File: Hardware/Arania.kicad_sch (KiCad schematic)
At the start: 9 parts, among them J14 LASER, J25 Alimentacion, J26 Masa, J7 Salidas, Q1 MMBT3904

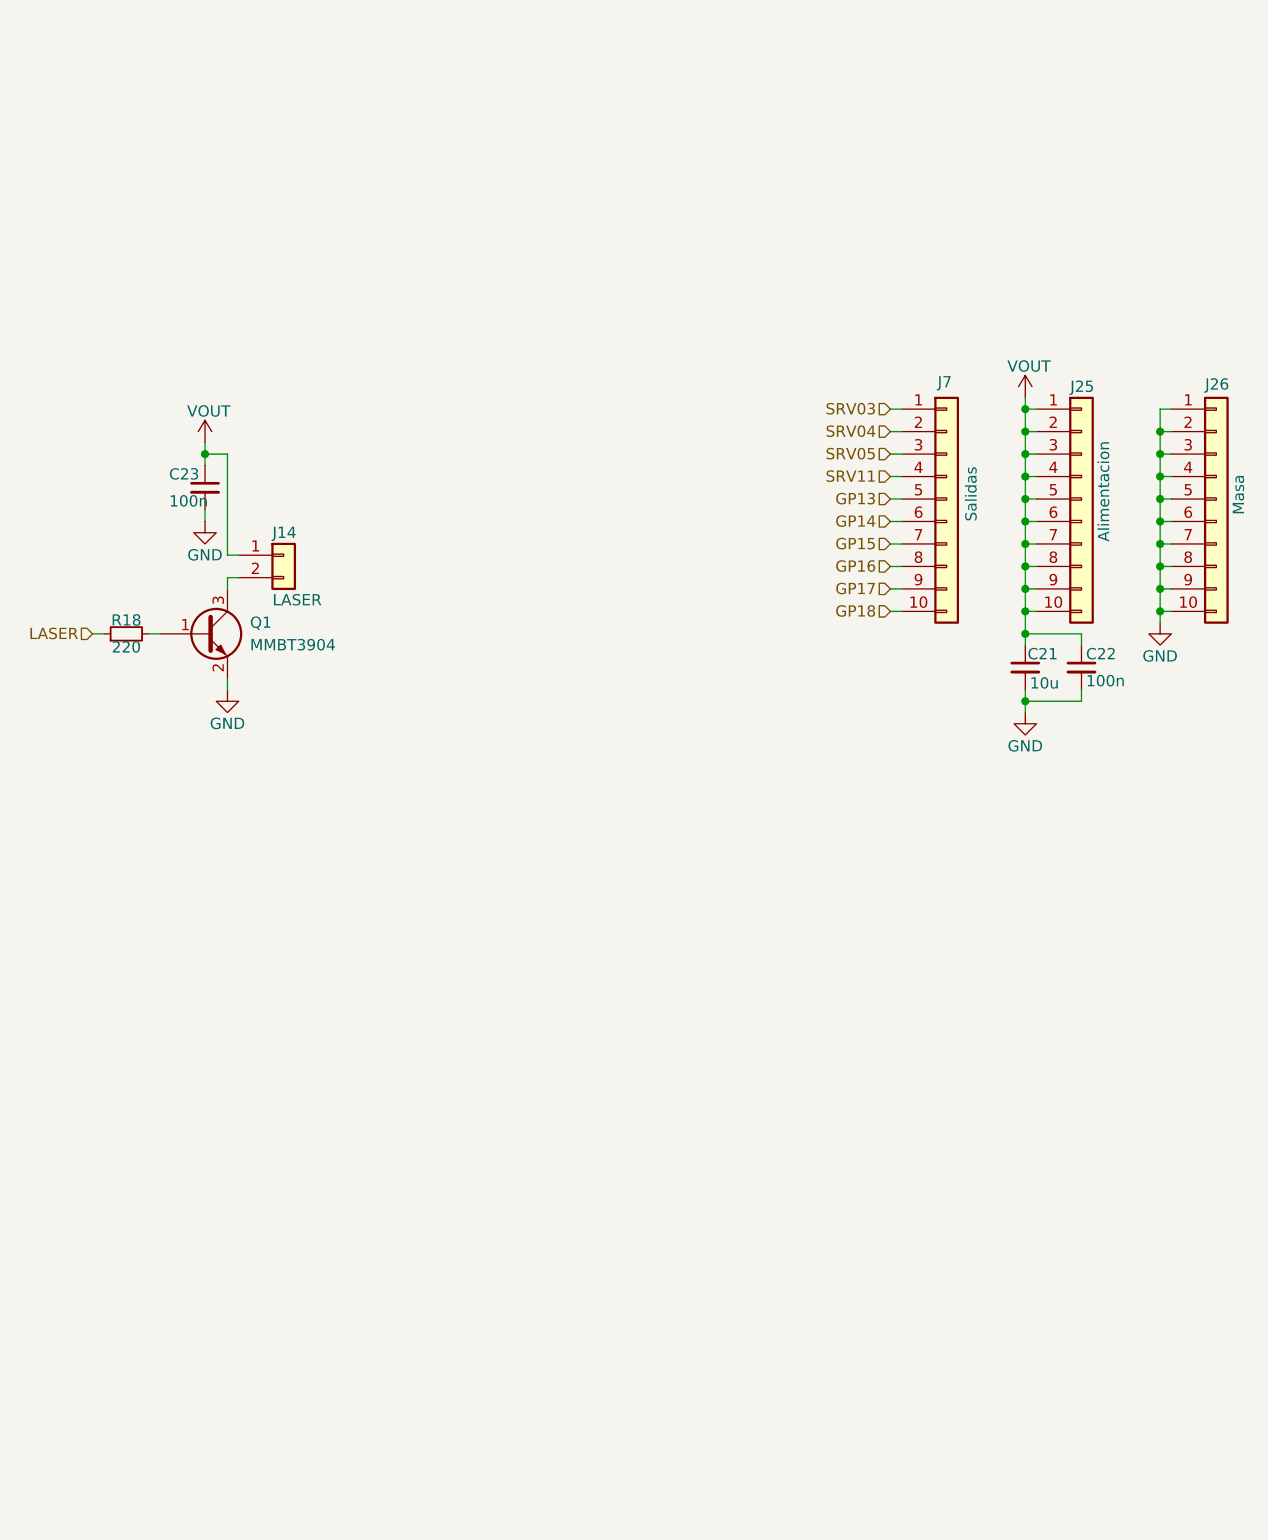
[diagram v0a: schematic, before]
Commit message: Cambio todos los conectores a SMD
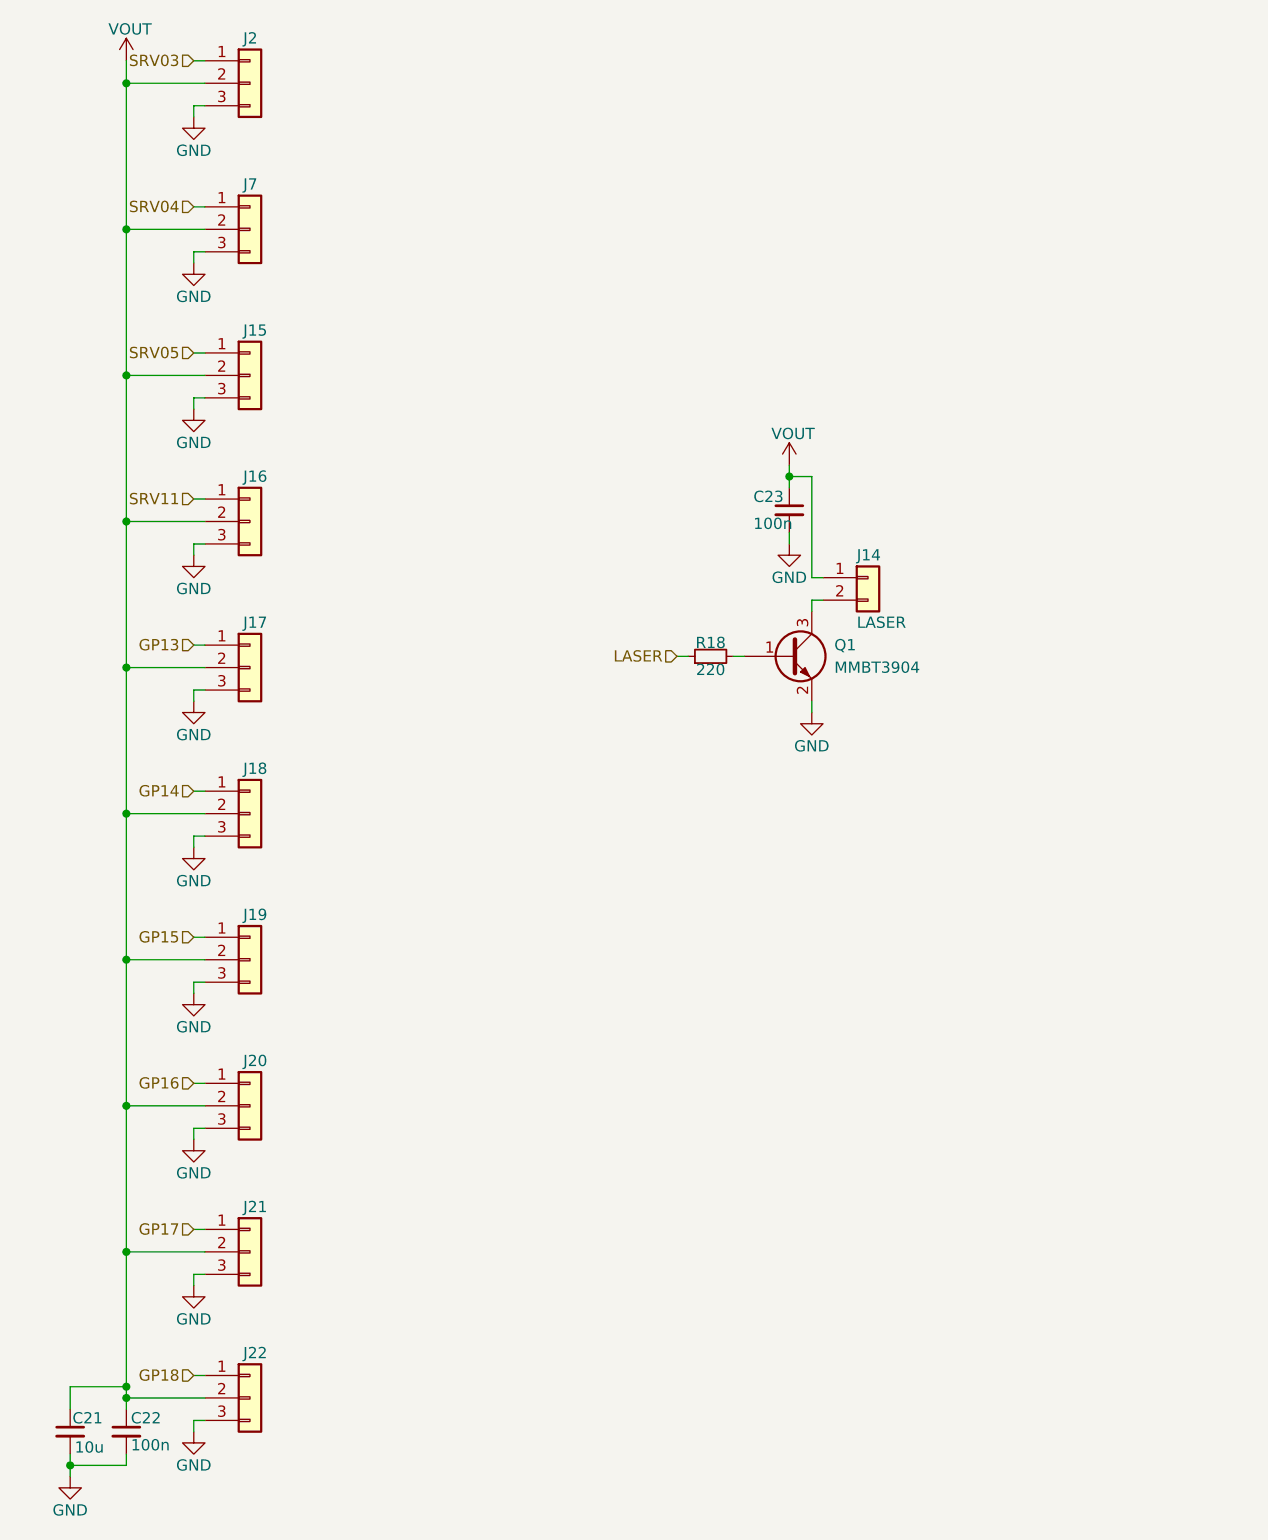
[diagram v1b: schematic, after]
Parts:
- removed J25: Alimentacion, Connector_PinHeader_2.54mm:PinHeader_1x10_P2.54mm_Vertical, symbol Connector_Generic:Conn_01x10
- removed J26: Masa, Connector_PinHeader_2.54mm:PinHeader_1x10_P2.54mm_Vertical, symbol Connector_Generic:Conn_01x10
- removed J7: Salidas, Connector_PinHeader_2.54mm:PinHeader_1x10_P2.54mm_Vertical, symbol Connector_Generic:Conn_01x10
- added J15, J16, J17, J18, J19, J2, J20, J21, J22, J7: Conn_01x03, footprints:SAMTEC_TSM-103-01-TM-SV-P-TR, symbol Connector_Generic:Conn_01x03
- J14: footprint Connector_PinHeader_2.54mm:PinHeader_1x02_P2.54mm_Vertical -> footprints:SAMTEC_SSM-102-L-SV-K-TR; PartNumber (none) -> SSM-102-L-SV-K-TR; PurchaseLink (none) -> https://www.digikey.com/en/products/detail/samtec-inc/SSM-1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
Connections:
- net GND: now also J15.3 (Pin_3), J16.3 (Pin_3), J17.3 (Pin_3), J18.3 (Pin_3), J19.3 (Pin_3), J2.3 (Pin_3), J20.3 (Pin_3), J21.3 (Pin_3), J22.3 (Pin_3), J7.3 (Pin_3)
- net GP13: now also J17.1 (Pin_1)
- net GP14: now also J18.1 (Pin_1)
- net GP15: now also J19.1 (Pin_1)
- net GP16: now also J20.1 (Pin_1)
- net GP17: now also J21.1 (Pin_1)
- net GP18: now also J22.1 (Pin_1)
- net SRV03: now also J2.1 (Pin_1)
- net SRV04: now also J7.1 (Pin_1)
- net SRV05: now also J15.1 (Pin_1)
- net SRV11: now also J16.1 (Pin_1)
- net VOUT: now also J15.2 (Pin_2), J16.2 (Pin_2), J17.2 (Pin_2), J18.2 (Pin_2), J19.2 (Pin_2), J2.2 (Pin_2), J20.2 (Pin_2), J21.2 (Pin_2), J22.2 (Pin_2), J7.2 (Pin_2)
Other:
- moved on the sheet: C21, C22, C23, J14, Q1, R18

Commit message: Correcciones en el ruteo, agrego fiduciales, 3D y serigrafía
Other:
- company: (none) -> Newsan
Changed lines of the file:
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@@
 	(title_block
 		(title "Archi Bot")
-		(date "2024-07-18")
-		(rev "1.1")
+		(date "2024-09-27")
+		(rev "1.2")
+		(company "Newsan")
 	)
 	(junction

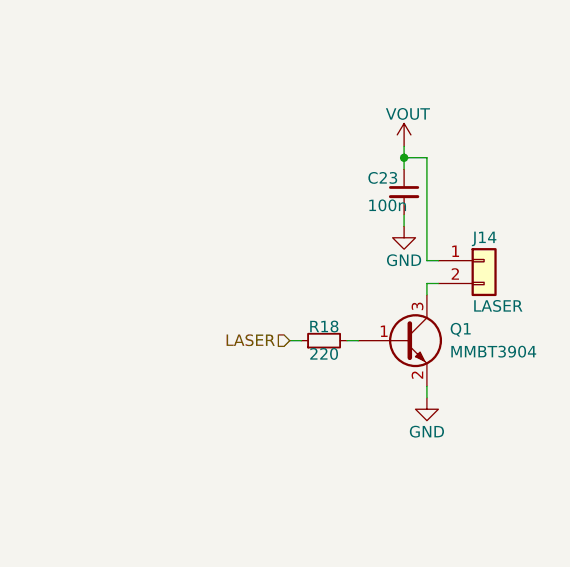
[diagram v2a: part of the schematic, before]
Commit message: Agrego test points, cambio conectores, finalizo v1.2
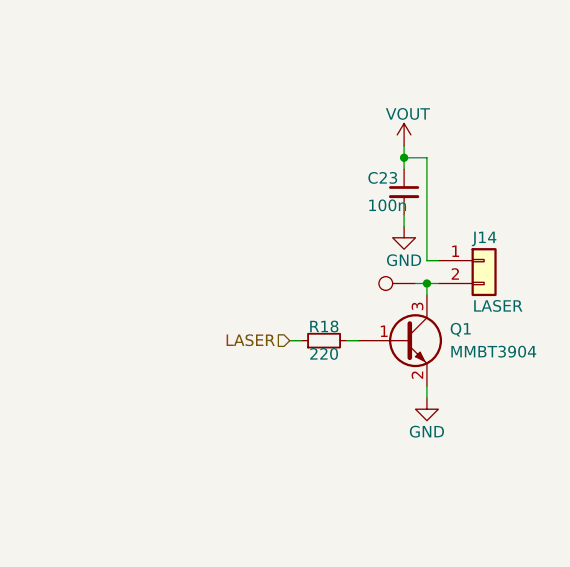
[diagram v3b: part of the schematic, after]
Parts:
- added TP28: TestPoint, TestPoint:TestPoint_Pad_D1.0mm, symbol Connector:TestPoint
- J14: footprint footprints:SAMTEC_SSM-102-L-SV-K-TR -> footprints:SAMTEC_SSM-102-L-SV-K-TR_modif
- J15, J16, J17, J18, J19, J2, J20, J21, J22, J7: footprint footprints:SAMTEC_TSM-103-01-TM-SV-P-TR -> footprints:SAMTEC_TSM-103-01-TM-SV-P-TR_modif
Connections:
- net at J14.2 (Pin_2), Q1.3 (C): now also TP28.1
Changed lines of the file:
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@@
+	)
+	(junction
+		(at 182.88 87.63)
+		(diameter 0)
+		(color 0 0 0 0)
 	)
 	(junction
@@
 		(pts
 			(xy 114.3 180.34) (xy 113.03 180.34)
+		)
+		(stroke
+			(width 0)
+			(type default)
+		)
+	)
+	(wire
+		(pts
+			(xy 181.61 87.63) (xy 182.88 87.63)
 		)
 		(stroke
@@
 			)
 		)
-		(property "Footprint" "footprints:SAMTEC_TSM-103-01-TM-SV-P-TR"
+		(property "Footprint" "footprints:SAMTEC_TSM-103-01-TM-SV-P-TR_modif"
 			(at 119.38 144.78 0)
 			(effects
@@
 				(path "/e63e39d7-6ac0-4ffd-8aa3-1841a4541b55/2971addb-a03b-4f30-bc70-6bc63fae2c84"
 					(reference "J20")
+					(unit 1)
+				)
+			)
+		)
+	)
+	(symbol
+		(lib_id "Connector:TestPoint")
+		(at 181.61 87.63 90)
+		(unit 1)
+		(exclude_from_sim no)
+		(in_bom yes)
+		(on_board yes)
+		(dnp no)
+		(fields_autoplaced yes)
+		(property "Reference" "TP28"
+			(at 177.0379 85.09 0)
+			(effects
+				(font
+					(size 1.27 1.27)
+				)
+				(justify left)
+				(hide yes)
+			)
+		)
+		(property "Value" "TestPoint"
+			(at 179.5779 85.09 0)
+			(effects
+				(font
+					(size 1.27 1.27)
+				)
+				(justify left)
+				(hide yes)
+			)
+		)
+		(property "Footprint" "TestPoint:TestPoint_Pad_D1.0mm"
+			(at 181.61 82.55 0)
+			(effects
+				(font
+					(size 1.27 1.27)
+				)
+				(hide yes)
+			)
+		)
+		(property "Datasheet" "~"
+			(at 181.61 82.55 0)
+			(effects
+				(font
+					(size 1.27 1.27)
+				)
+				(hide yes)
+			)
+		)
+		(property "Description" "test point"
+			(at 181.61 87.63 0)
+			(effects
+				(font
+					(size 1.27 1.27)
+				)
+				(hide yes)
+			)
+		)
+		(pin "1"
+		)
+		(instances
+			(project "ArchiBot"
+				(path "/e63e39d7-6ac0-4ffd-8aa3-1841a4541b55/2971addb-a03b-4f30-bc70-6bc63fae2c84"
+					(reference "TP28")
 					(unit 1)
 				)
@@
 			)
 		)
-		(property "Footprint" "footprints:SAMTEC_TSM-103-01-TM-SV-P-TR"
+		(property "Footprint" "footprints:SAMTEC_TSM-103-01-TM-SV-P-TR_modif"
 			(at 119.38 128.27 0)
 			(effects
@@
 			)
 		)
-		(property "Footprint" "footprints:SAMTEC_TSM-103-01-TM-SV-P-TR"
+		(property "Footprint" "footprints:SAMTEC_TSM-103-01-TM-SV-P-TR_modif"
 			(at 119.38 111.76 0)
 			(effects
@@
 			)
 		)
-		(property "Footprint" "footprints:SAMTEC_TSM-103-01-TM-SV-P-TR"
+		(property "Footprint" "footprints:SAMTEC_TSM-103-01-TM-SV-P-TR_modif"
 			(at 119.38 45.72 0)
 			(effects
@@
 			)
 		)
-		(property "Footprint" "footprints:SAMTEC_TSM-103-01-TM-SV-P-TR"
+		(property "Footprint" "footprints:SAMTEC_TSM-103-01-TM-SV-P-TR_modif"
 			(at 119.38 78.74 0)
 			(effects
@@
 			)
 		)
-		(property "Footprint" "footprints:SAMTEC_TSM-103-01-TM-SV-P-TR"
+		(property "Footprint" "footprints:SAMTEC_TSM-103-01-TM-SV-P-TR_modif"
 			(at 119.38 62.23 0)
 			(effects
@@
 			)
 		)
-		(property "Footprint" "footprints:SAMTEC_TSM-103-01-TM-SV-P-TR"
+		(property "Footprint" "footprints:SAMTEC_TSM-103-01-TM-SV-P-TR_modif"
 			(at 119.38 161.29 0)
 			(effects
@@
 			)
 		)
-		(property "Footprint" "footprints:SAMTEC_TSM-103-01-TM-SV-P-TR"
+		(property "Footprint" "footprints:SAMTEC_TSM-103-01-TM-SV-P-TR_modif"
 			(at 119.38 95.25 0)
 			(effects
@@
 			)
 		)
-		(property "Footprint" "footprints:SAMTEC_SSM-102-L-SV-K-TR"
+		(property "Footprint" "footprints:SAMTEC_SSM-102-L-SV-K-TR_modif"
 			(at 189.23 85.09 0)
 			(effects
@@
 			)
 		)
-		(property "Footprint" "footprints:SAMTEC_TSM-103-01-TM-SV-P-TR"
+		(property "Footprint" "footprints:SAMTEC_TSM-103-01-TM-SV-P-TR_modif"
 			(at 119.38 177.8 0)
 			(effects
@@
 			)
 		)
-		(property "Footprint" "footprints:SAMTEC_TSM-103-01-TM-SV-P-TR"
+		(property "Footprint" "footprints:SAMTEC_TSM-103-01-TM-SV-P-TR_modif"
 			(at 119.38 29.21 0)
 			(effects

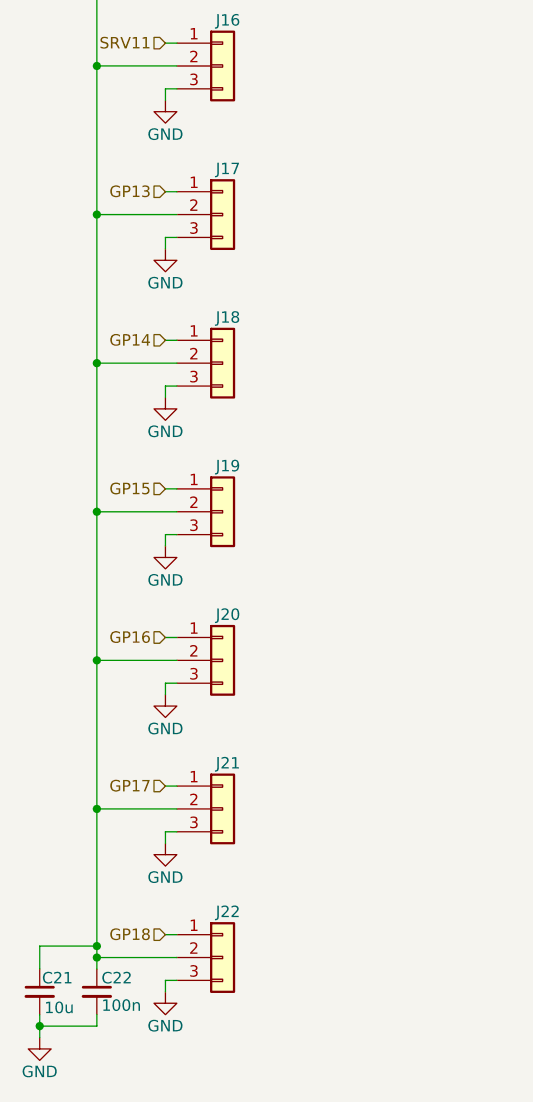
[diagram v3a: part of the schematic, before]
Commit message: Agrego testpoints y modifico footprint de bornera
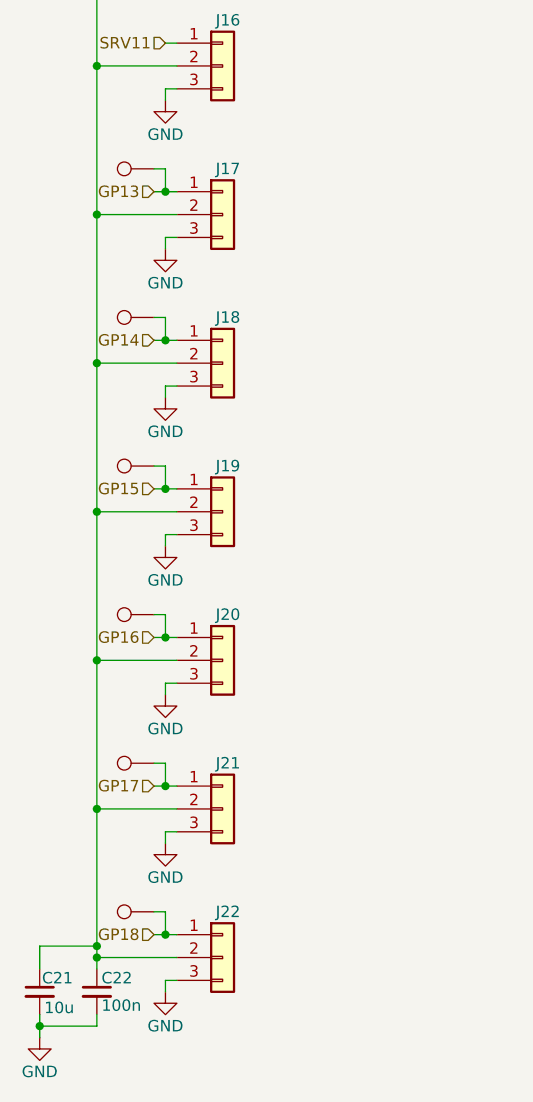
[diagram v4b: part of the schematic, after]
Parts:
- added TP39, TP40, TP41, TP42, TP43, TP44: TestPoint, TestPoint:TestPoint_Pad_D1.0mm, symbol Connector:TestPoint
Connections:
- net GP13: now also TP39.1
- net GP14: now also TP40.1
- net GP15: now also TP41.1
- net GP16: now also TP42.1
- net GP17: now also TP43.1
- net GP18: now also TP44.1

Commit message: Agrego campos manufacturer y package
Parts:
- C21: Manufacturer (none) -> Murata Electronics; Package (none) -> 0805 (2012 Metric)
- C22, C23: Manufacturer (none) -> Samsung Electro-Mechanics; Package (none) -> 0603 (1608 Metric)
- J14: Manufacturer (none) -> Samtec Inc.; Package (none) -> 2POS 0.100" (2.54mm)
- J15, J16, J17, J18, J19, J2, J20, J21, J22, J7: Manufacturer (none) -> Samtec Inc.; Package (none) -> 3POS 0.100" (2.54mm)
- Q1: Manufacturer (none) -> Diotec Semiconductor; Package (none) -> TO-236-3, SC-59, SOT-23-3
- R18: Manufacturer (none) -> YAGEO; Package (none) -> 0603 (1608 Metric)
